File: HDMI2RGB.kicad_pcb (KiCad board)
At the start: 2 copper layers, 44 parts, among them J1 HDMI_A, J2 QTH-030-02-L-DA, U5 ADV7611

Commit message: Added pdata lines and ran bus connections
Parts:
- added RP1: R_PACK8, rpack:RPACK-8_0616, F.Cu at (75.4, 68.2)
- added RP2: R_PACK8, rpack:RPACK-8_0616, F.Cu at (86.8, 83.6)
- added RP3: R_PACK8, rpack:RPACK-8_0616, F.Cu at (94.2, 96.8)
- moved J2 22.3 mm to (79.2, 75.5)
- moved J1 14.7 mm to (76.8, 131.2)
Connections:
- net DATEN renamed PCLK
- J2 pad 1: Net-(J2-Pad1) -> /CONNECTOR/PDATA1
- J2 pad 10: Net-(J2-Pad10) -> /CONNECTOR/PDATA12
- J2 pad 11: Net-(J2-Pad11) -> /CONNECTOR/PDATA2
- J2 pad 12: Net-(J2-Pad12) -> /CONNECTOR/PDATA14
- J2 pad 13: Net-(J2-Pad13) -> /CONNECTOR/PDATA4
- J2 pad 14: Net-(J2-Pad14) -> /CONNECTOR/PDATA16
- J2 pad 15: Net-(J2-Pad15) -> /CONNECTOR/PDATA6
- J2 pad 16: Net-(J2-Pad16) -> /CONNECTOR/PDATA18
- J2 pad 18: Net-(J2-Pad18) -> /CONNECTOR/PDATA20
- J2 pad 20: Net-(J2-Pad20) -> /CONNECTOR/PDATA22
- J2 pad 21: Net-(J2-Pad21) -> /CONNECTOR/PDATA11
- J2 pad 25: Net-(J2-Pad25) -> /CONNECTOR/PDATA13
- J2 pad 29: Net-(J2-Pad29) -> /CONNECTOR/PDATA15
- J2 pad 3: Net-(J2-Pad3) -> /CONNECTOR/PDATA3
- J2 pad 33: Net-(J2-Pad33) -> /CONNECTOR/PDATA17
- J2 pad 37: Net-(J2-Pad37) -> /CONNECTOR/PDATA19
- J2 pad 4: Net-(J2-Pad4) -> /CONNECTOR/PDATA8
- J2 pad 41: Net-(J2-Pad41) -> /CONNECTOR/PDATA21
- J2 pad 45: Net-(J2-Pad45) -> /CONNECTOR/PDATA23
- J2 pad 5: Net-(J2-Pad5) -> /CONNECTOR/PDATA5
- J2 pad 6: Net-(J2-Pad6) -> /CONNECTOR/PDATA9
- J2 pad 7: Net-(J2-Pad7) -> /CONNECTOR/PDATA7
- J2 pad 8: Net-(J2-Pad8) -> /CONNECTOR/PDATA10
- J2 pad 9: Net-(J2-Pad9) -> /CONNECTOR/PDATA0

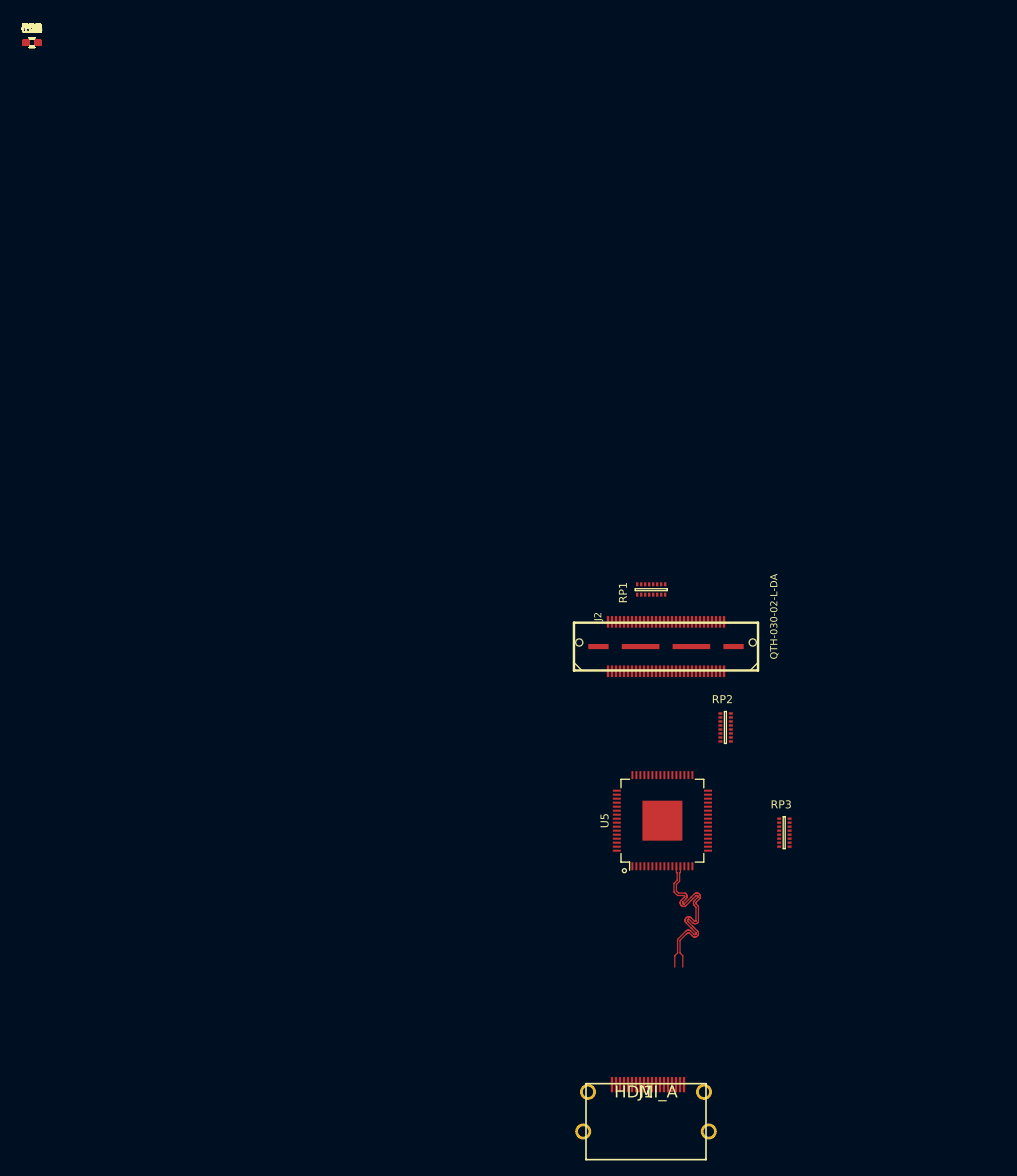
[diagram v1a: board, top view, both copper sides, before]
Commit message: Started PCB Layout, added mounting holes, connectors, in correct locations
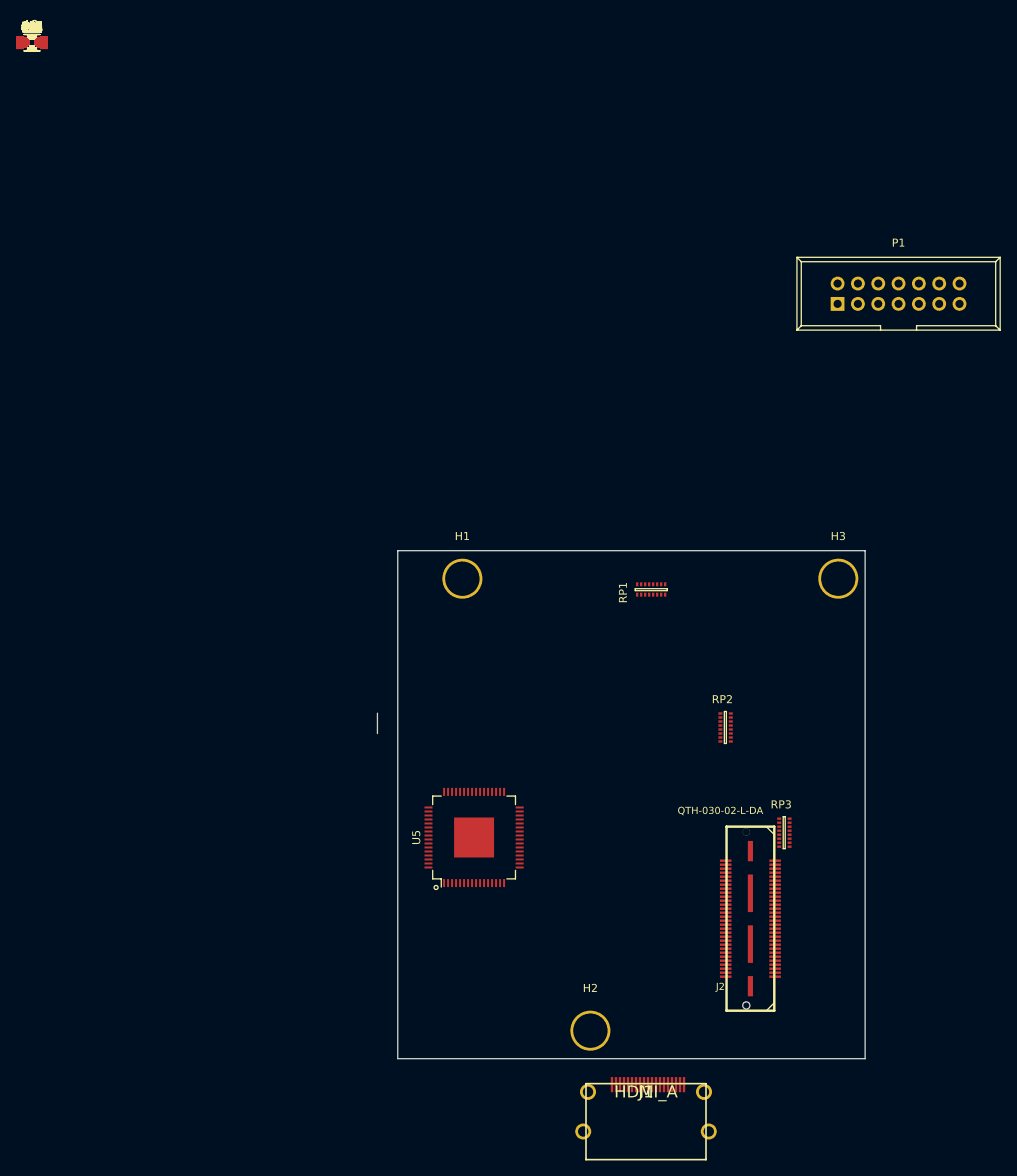
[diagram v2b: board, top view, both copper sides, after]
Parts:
- added C13, C14: 18pF, Capacitors_SMD:C_0603, F.Cu at (0.00, 0.00)
- added C29, C30, C31, C32, C33, C34, C35: 0.1uF, Capacitors_SMD:C_0402, F.Cu at (0.00, 0.00)
- added C36, C37, C40, C41: 10uF, Capacitors_SMD:C_0805, F.Cu at (0.00, 0.00)
- added C38, C39: 4.7uF, Capacitors_SMD:C_0805, F.Cu at (0.00, 0.00)
- added D1, D2, D3, D4: LED, Capacitors_SMD:C_0603, F.Cu at (0.00, 0.00)
- added H1: HOLE1, Mounting_Holes:MountingHole_4.3mm_M4_Pad, F.Cu at (53.8, 67.0)
- added H2: HOLE1, Mounting_Holes:MountingHole_4.3mm_M4_Pad, F.Cu at (69.8, 123.5)
- added H3: HOLE1, Mounting_Holes:MountingHole_4.3mm_M4_Pad, F.Cu at (100.8, 67.0)
- added L1, L2: 2.2uH, Capacitors_SMD:C_1206, F.Cu at (0.00, 0.00)
- added P1: CONN_02X07, Connect:IDC_Header_Straight_14pins, F.Cu at (100.7, 32.6)
- added R11, R15, R16: 0.0, Resistors_SMD:R_0402, F.Cu at (0.00, 0.00)
- added R12, R13, R14, R17, R18, R19, R20, R21, R22, R23: 4.7k, Resistors_SMD:R_0402, F.Cu at (0.00, 0.00)
- added R24, R25, R26: 270, Resistors_SMD:R_0402, F.Cu at (0.00, 0.00)
- added R27: 200, Resistors_SMD:R_0805, F.Cu at (0.00, 0.00)
- added R28: 270, Resistors_SMD:R_0603, F.Cu at (0.00, 0.00)
- added R29, R30: 150k, Resistors_SMD:R_0603, F.Cu at (0.00, 0.00)
- added R32: 300k, Resistors_SMD:R_0603, F.Cu at (0.00, 0.00)
- added R33: 680k, Resistors_SMD:R_0603, F.Cu at (0.00, 0.00)
- moved J2 35.6 mm to (89.8, 109.5), turned to 90 degrees
- moved U5 23.6 mm to (55.3, 99.3)
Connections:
- net Net-(J2-Pad31) renamed 3DR
- net Net-(J2-Pad35) renamed HOST_IRQ
- net Net-(J2-Pad36) renamed PROJ_ON
- net Net-(J2-Pad39) renamed I2C0_SDA
- net Net-(J2-Pad43) renamed I2C0_SCL
- net Net-(J2-Pad46) renamed SPI0_CLK
- net Net-(J2-Pad47) renamed SPI0_MISO
- net Net-(J2-Pad49) renamed SPI0_MOSI
- net Net-(J2-Pad51) renamed SPI0_CSZ0
- net Net-(J2-Pad53) renamed /CONNECTOR/RESETZ
- net RESET_ADV renamed RESET_ADV7611
- J2 pad 17: Net-(J2-Pad17) -> DATEN_CMD
- J2 pad 19: Net-(J2-Pad19) -> PCLK
- J2 pad 2: Net-(J2-Pad2) -> VSYNC_WE
- J2 pad 27: Net-(J2-Pad27) -> HSYNC_CS
- J2 pad 48: Net-(J2-Pad48) -> +1V8
- J2 pad 50: Net-(J2-Pad50) -> +3V3
- J2 pad 52: Net-(J2-Pad52) -> +1V8
- J2 pad 55: Net-(J2-Pad55) -> SYSPWR
- J2 pad 56: Net-(J2-Pad56) -> SYSPWR
- J2 pad 57: Net-(J2-Pad57) -> SYSPWR
- J2 pad 58: Net-(J2-Pad58) -> SYSPWR
- J2 pad 59: Net-(J2-Pad59) -> SYSPWR
- J2 pad 60: Net-(J2-Pad60) -> SYSPWR
- J2 pad 61: Net-(J2-Pad61) -> GND
- J2 pad 62: Net-(J2-Pad62) -> GND
- J2 pad 63: Net-(J2-Pad63) -> GND
- J2 pad 64: Net-(J2-Pad64) -> GND
- U5 pad 3: Net-(U5-Pad3) -> /HDMI_INPUT/HDMI_CLK_N
- U5 pad 4: Net-(U5-Pad4) -> /HDMI_INPUT/HDMI_CLK_P
- U5 pad 45: PCLK -> DATEN_CMD
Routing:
- net /HDMI_INPUT/HDMI_RX2_N: track 23.2 -> 0.00 mm
- net /HDMI_INPUT/HDMI_RX2_P: track 23.2 -> 0.00 mm
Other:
- board outline added: 61 x 63.5 mm

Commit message: Hdmi and RGB is routed, waiting for trace matching
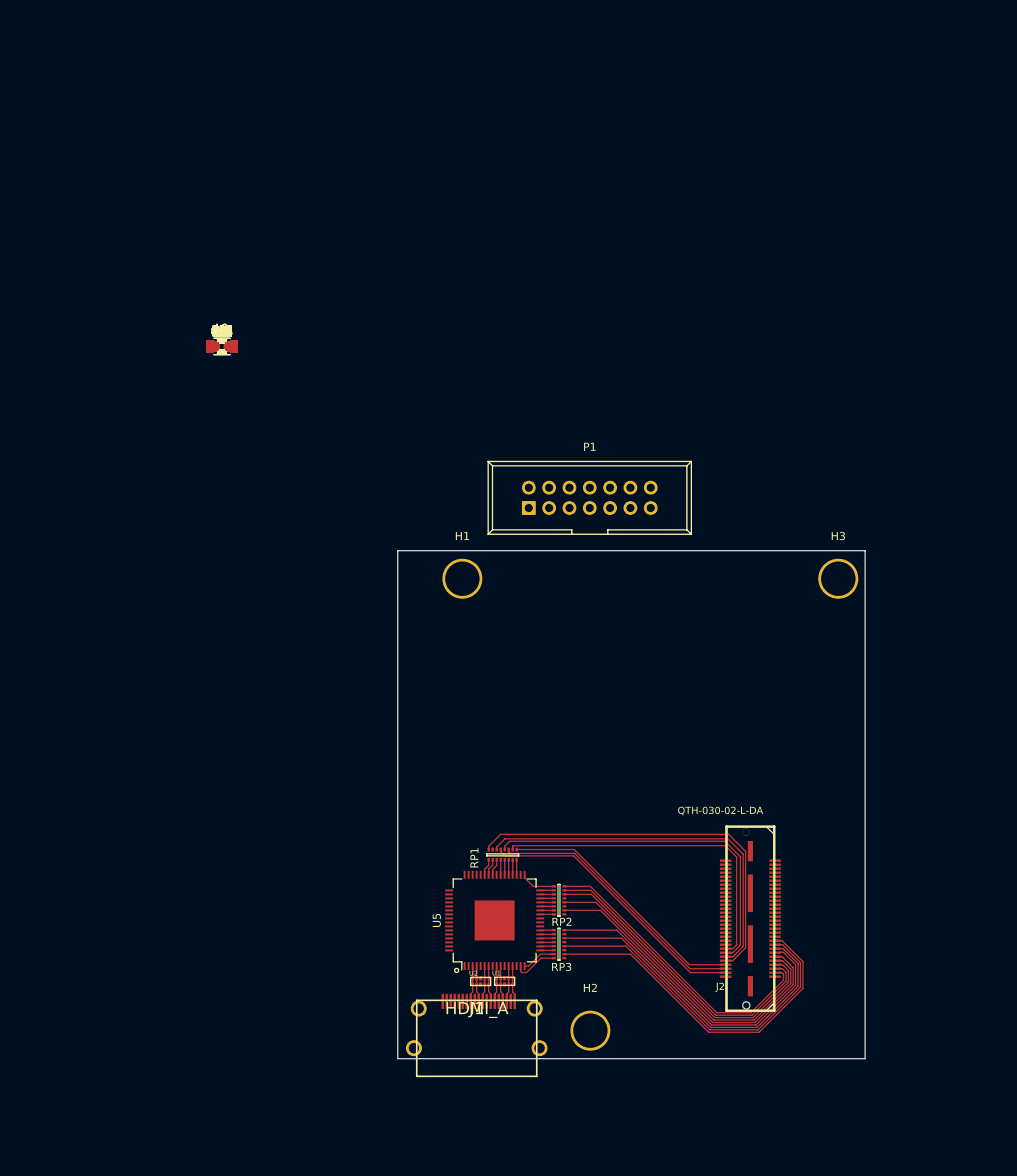
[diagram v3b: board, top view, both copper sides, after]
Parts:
- added U1: TPD4S010DQAR, misc:10-USON, F.Cu at (59.1, 117.3)
- added U2: TPD4S010DQAR, misc:10-USON, F.Cu at (56.1, 117.3)
- moved P1 46.3 mm to (62.1, 58.2)
- moved C1 44.8 mm to (23.7, 38.0)
- moved C10 44.8 mm to (23.7, 38.0)
- moved C11 44.8 mm to (23.7, 38.0)
- moved C12 44.8 mm to (23.7, 38.0)
- moved C13 44.8 mm to (23.7, 38.0)
- moved C14 44.8 mm to (23.7, 38.0)
- moved C15 44.8 mm to (23.7, 38.0)
- moved C16 44.8 mm to (23.7, 38.0)
- moved C17 44.8 mm to (23.7, 38.0)
- moved C18 44.8 mm to (23.7, 38.0)
- moved C19 44.8 mm to (23.7, 38.0)
- moved C2 44.8 mm to (23.7, 38.0)
- moved C20 44.8 mm to (23.7, 38.0)
- moved C21 44.8 mm to (23.7, 38.0)
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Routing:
- net /CONNECTOR/PDATA0: track 0.00 -> 49.2 mm
- net /CONNECTOR/PDATA2: track 0.00 -> 46.6 mm
- net /CONNECTOR/PDATA4: track 0.00 -> 44.2 mm
- net /CONNECTOR/PDATA22: track 0.00 -> 44.1 mm
- net /CONNECTOR/PDATA20: track 0.00 -> 43.2 mm
- net /CONNECTOR/PDATA18: track 0.00 -> 42.4 mm
- net /CONNECTOR/PDATA6: track 0.00 -> 41.6 mm
- net /CONNECTOR/PDATA14: track 0.00 -> 41.3 mm
- net /CONNECTOR/PDATA16: track 0.00 -> 41.2 mm
- net /CONNECTOR/PDATA12: track 0.00 -> 40.5 mm
- net /CONNECTOR/PDATA10: track 0.00 -> 39.6 mm
- net /CONNECTOR/PDATA9: track 0.00 -> 38.6 mm
- net /CONNECTOR/PDATA8: track 0.00 -> 37.5 mm
- net /CONNECTOR/PDATA3: track 0.00 -> 34.6 mm
- net /CONNECTOR/PDATA5: track 0.00 -> 33.5 mm
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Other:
- board size 61 x 63.5 mm -> 58.4 x 63.5 mm
- copper layers 2 -> 4
- net class Default: clearance 0.2 -> 0.1524; trace_width 0.25 -> 0.1524; via_dia 0.6 -> 0.5842; via_drill 0.4 -> 0.381
- rule trace_clearance: 0.2 -> 0.1524
- rule trace_min: 0.2 -> 0.1524
- rule via_min_drill: 0.3 -> 0.381
- rule via_min_size: 0.4 -> 0.5842

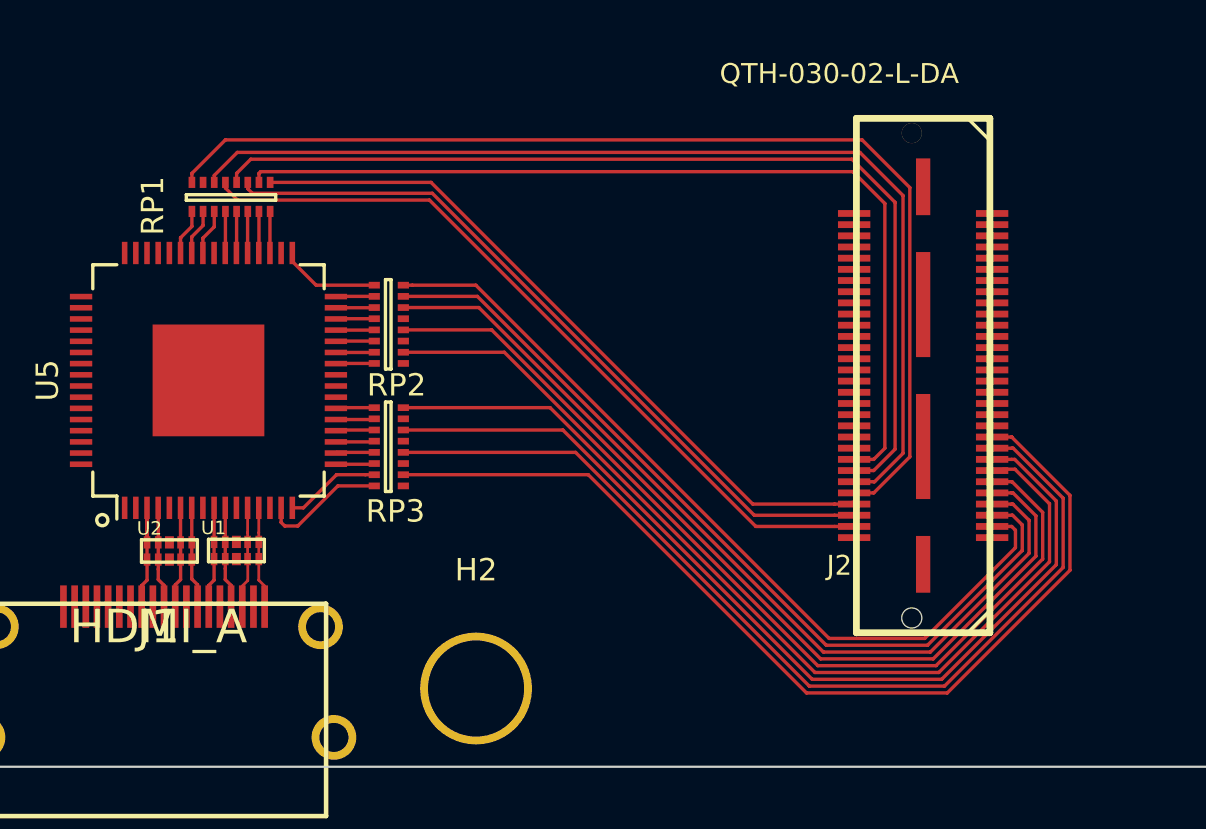
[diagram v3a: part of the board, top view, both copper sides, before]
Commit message: Hdmi and RGB is routed, waiting for trace matching
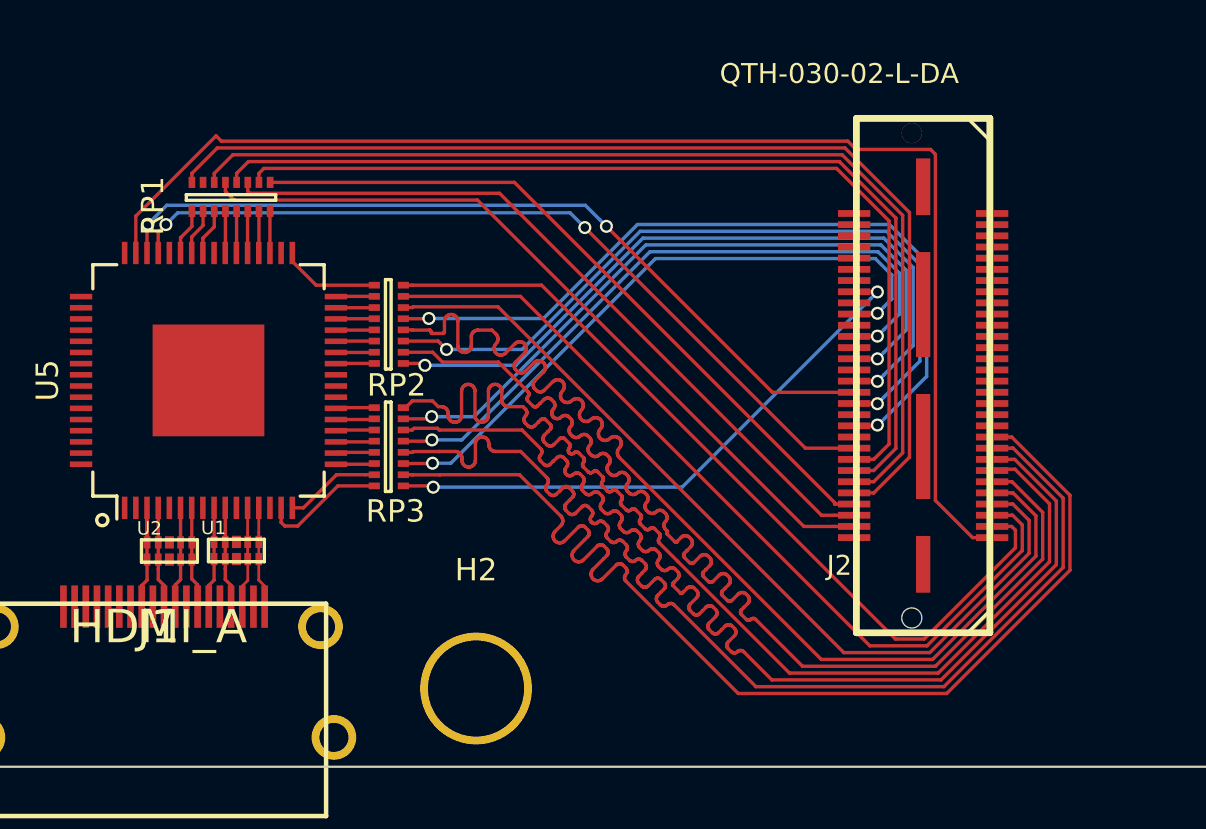
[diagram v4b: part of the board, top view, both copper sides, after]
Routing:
- net VSYNC_WE: track 0.00 -> 58.0 mm
- net DATEN_CMD: track 0.00 -> 36.8 mm, vias 0 -> 2
- net HSYNC_CS: track 0.00 -> 36.7 mm, vias 0 -> 2
- net /CONNECTOR/PDATA11: track 0.00 -> 35.2 mm, vias 0 -> 2
- net /CONNECTOR/PDATA13: track 0.00 -> 34.1 mm, vias 0 -> 2
- net /CONNECTOR/PDATA15: track 0.00 -> 32.5 mm, vias 0 -> 2
- net /CONNECTOR/PDATA17: track 0.00 -> 31.7 mm, vias 0 -> 2
- net /CONNECTOR/PDATA19: track 0.00 -> 30.4 mm, vias 0 -> 2
- net /CONNECTOR/PDATA21: track 0.00 -> 29.3 mm, vias 0 -> 2
- net /CONNECTOR/PDATA23: track 0.00 -> 25.9 mm, vias 0 -> 2
- net /CONNECTOR/PDATA12: track 40.5 -> 50.6 mm
- net /CONNECTOR/PDATA16: track 41.2 -> 50.8 mm
- net /CONNECTOR/PDATA14: track 41.3 -> 50.8 mm
- net /CONNECTOR/PDATA18: track 42.4 -> 50.9 mm
- net /CONNECTOR/PDATA20: track 43.2 -> 50.9 mm
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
